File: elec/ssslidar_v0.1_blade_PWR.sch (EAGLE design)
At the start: 22 parts, among them P1 PIN_SMD_0.8X1_RECT, P10 PIN_SMD_0.8X1_RECT, P11 PIN_SMD_1X1_RECT, P12 PIN_SMD_0.8X1_RECT, P13 PIN_SMD_0.8X1_RECT, P16 PIN_SMD_0.8X1_RECT, P17 PIN_SMD_1X1_RECT, P18 PIN_SMD_0.8X1_RECT, P2 PIN_SMD_1X1_RECT, P3 PIN_SMD_0.8X1_RECT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

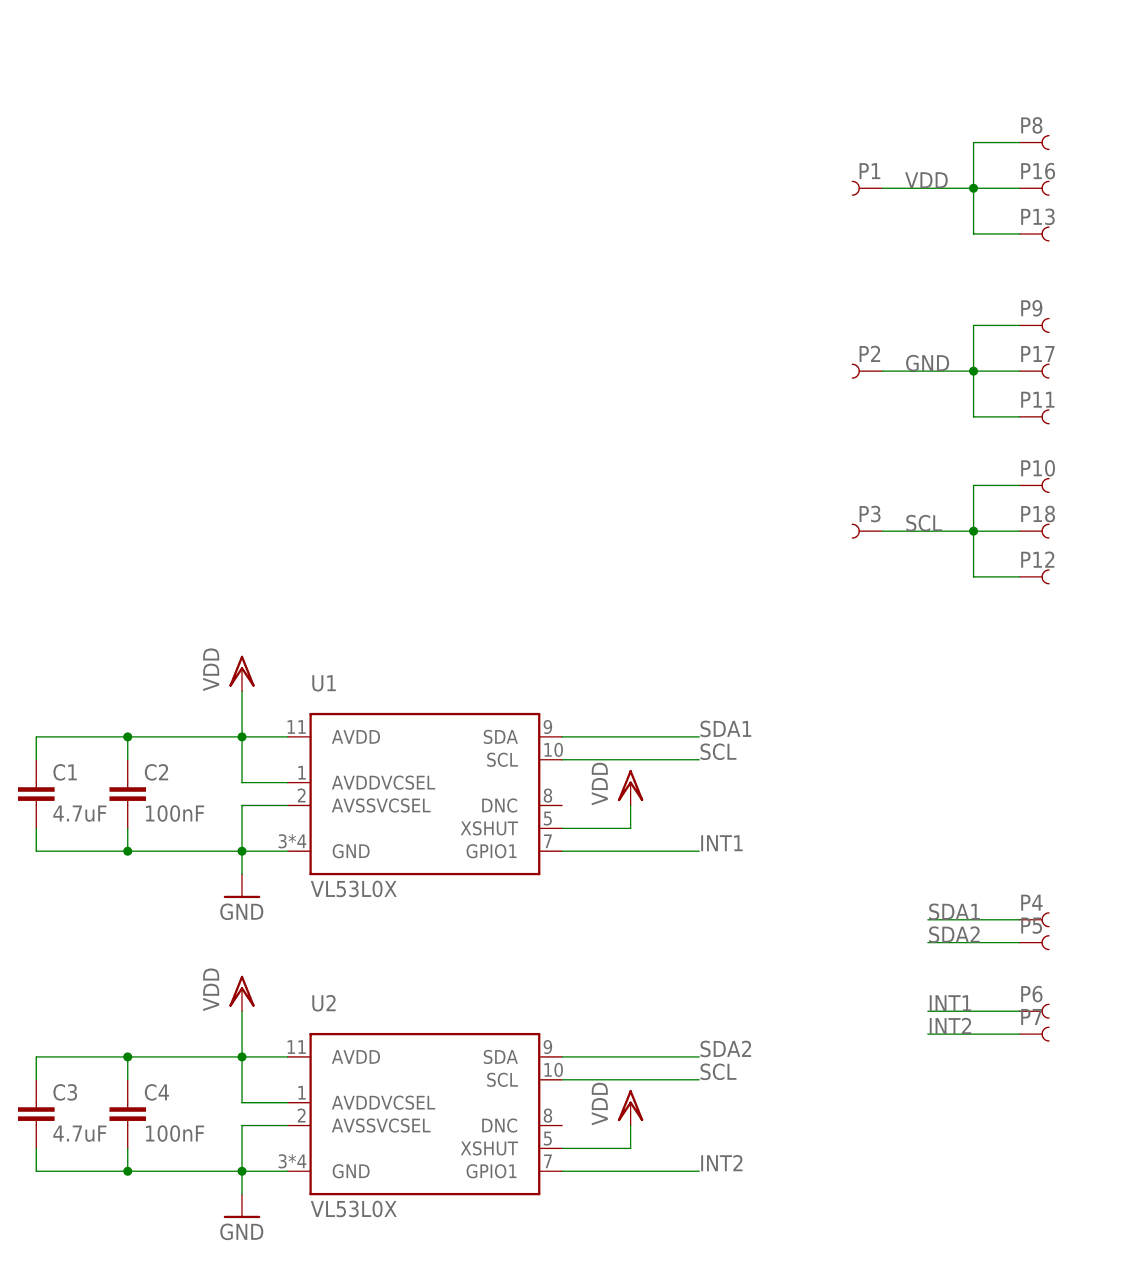
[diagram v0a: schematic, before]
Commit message: Working on main board Made blades longer to avoid too much occlusion from the main PCB (but we will still need to put the whole thing on a mast).
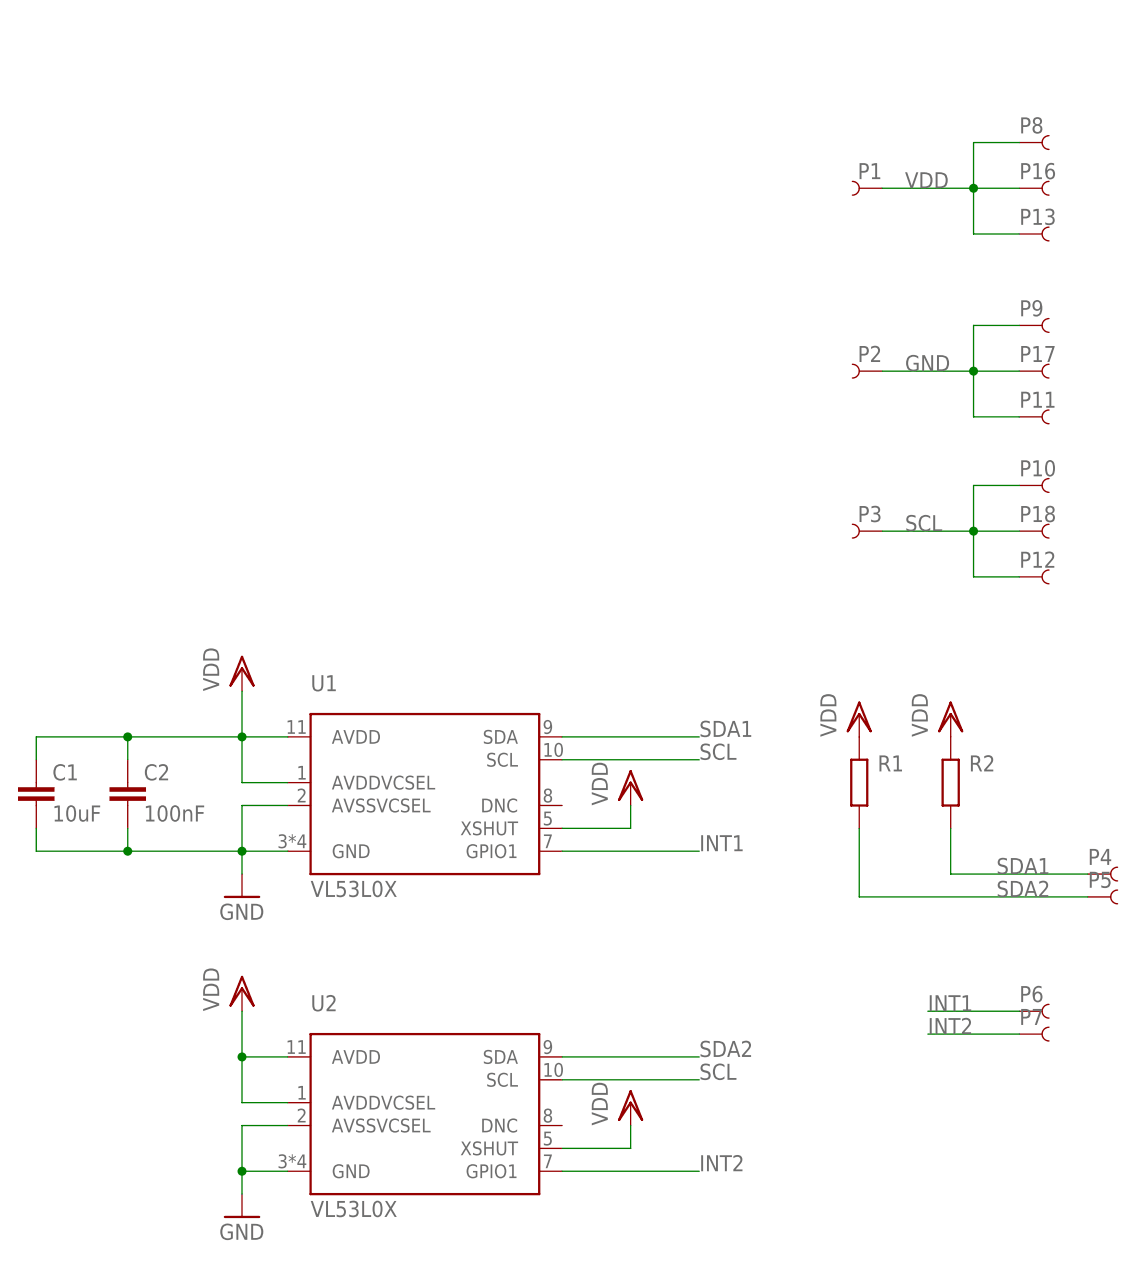
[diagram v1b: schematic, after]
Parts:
- removed C3: 4.7uF, Xevelabs:C0603
- removed C4: 100nF, Xevelabs:C0201
- added R1, R2: (no value), Xevelabs:R0402
- C1: value 4.7uF -> 10uF; device Xevelabs:C0603 -> Xevelabs:C0805
- C2: device Xevelabs:C0201 -> Xevelabs:C0402
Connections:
- net GND: no longer C3.2, C4.2
- net SDA1: now also R2.1
- net SDA2: now also R1.1
- net VDD: now also R1.2, R2.2; no longer C3.1, C4.1
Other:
- moved on the sheet: P4, P5
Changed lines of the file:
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@@
 <part name="GND1" library="supply1" deviceset="GND" device=""/>
 <part name="VDD1" library="supply1" deviceset="VDD" device=""/>
-<part name="C1" library="Xevelabs" deviceset="C" device="0603" value="4.7uF"/>
-<part name="C2" library="Xevelabs" deviceset="C" device="0201" value="100nF"/>
+<part name="C1" library="Xevelabs" deviceset="C" device="0805" value="10uF"/>
+<part name="C2" library="Xevelabs" deviceset="C" device="0402" value="100nF"/>
 <part name="VDD2" library="supply1" deviceset="VDD" device=""/>
 <part name="U2" library="VL53L0X" deviceset="VL53L0X" device=""/>
 <part name="GND2" library="supply1" deviceset="GND" device=""/>
 <part name="VDD3" library="supply1" deviceset="VDD" device=""/>
-<part name="C3" library="Xevelabs" deviceset="C" device="0603" value="4.7uF"/>
-<part name="C4" library="Xevelabs" deviceset="C" device="0201" value="100nF"/>
 <part name="VDD4" library="supply1" deviceset="VDD" device=""/>
 <part name="P1" library="Xevelabs" deviceset="PIN" device="_SMD_0.8X1_RECT" value="PIN_SMD_0.8X1_RECT"/>
@@
 <part name="P12" library="Xevelabs" deviceset="PIN" device="_SMD_0.8X1_RECT" value="PIN_SMD_0.8X1_RECT"/>
 <part name="P13" library="Xevelabs" deviceset="PIN" device="_SMD_0.8X1_RECT" value="PIN_SMD_0.8X1_RECT"/>
+<part name="R1" library="Xevelabs" deviceset="R" device="0402"/>
+<part name="R2" library="Xevelabs" deviceset="R" device="0402"/>
+<part name="VDD5" library="supply1" deviceset="VDD" device=""/>
+<part name="VDD6" library="supply1" deviceset="VDD" device=""/>
 </parts>
 <sheets>
@@
 <instance part="GND2" gate="1" x="27.94" y="5.08"/>
 <instance part="VDD3" gate="G$1" x="27.94" y="30.48"/>
-<instance part="C3" gate="G$1" x="5.08" y="15.24"/>
-<instance part="C4" gate="G$1" x="15.24" y="15.24"/>
 <instance part="VDD4" gate="G$1" x="71.12" y="17.78"/>
 <instance part="P1" gate="G$1" x="99.06" y="119.38" rot="MR0"/>
 <instance part="P2" gate="G$1" x="99.06" y="99.06" rot="MR0"/>
 <instance part="P3" gate="G$1" x="99.06" y="81.28" rot="MR0"/>
-<instance part="P4" gate="G$1" x="114.3" y="38.1"/>
-<instance part="P5" gate="G$1" x="114.3" y="35.56"/>
+<instance part="P4" gate="G$1" x="121.92" y="43.18"/>
+<instance part="P5" gate="G$1" x="121.92" y="40.64"/>
 <instance part="P6" gate="G$1" x="114.3" y="27.94"/>
 <instance part="P7" gate="G$1" x="114.3" y="25.4"/>
@@
 <instance part="P12" gate="G$1" x="114.3" y="76.2"/>
 <instance part="P13" gate="G$1" x="114.3" y="114.3"/>
+<instance part="R1" gate="G$1" x="96.52" y="53.34"/>
+<instance part="R2" gate="G$1" x="106.68" y="53.34"/>
+<instance part="VDD5" gate="G$1" x="96.52" y="60.96"/>
+<instance part="VDD6" gate="G$1" x="106.68" y="60.96"/>
 </instances>
 <busses>
@@
 <wire x1="27.94" y1="17.78" x2="27.94" y2="22.86" width="0.1524" layer="91"/>
 <junction x="27.94" y="22.86"/>
-<wire x1="27.94" y1="22.86" x2="15.24" y2="22.86" width="0.1524" layer="91"/>
-<pinref part="C4" gate="G$1" pin="1"/>
-<wire x1="15.24" y1="22.86" x2="15.24" y2="20.32" width="0.1524" layer="91"/>
-<pinref part="C3" gate="G$1" pin="1"/>
-<wire x1="15.24" y1="22.86" x2="5.08" y2="22.86" width="0.1524" layer="91"/>
-<wire x1="5.08" y1="22.86" x2="5.08" y2="20.32" width="0.1524" layer="91"/>
-<junction x="15.24" y="22.86"/>
 </segment>
 <segment>
@@
 <pinref part="P13" gate="G$1" pin="1"/>
 <wire x1="109.22" y1="114.3" x2="114.3" y2="114.3" width="0.1524" layer="91"/>
+</segment>
+<segment>
+<pinref part="R1" gate="G$1" pin="2"/>
+<pinref part="VDD5" gate="G$1" pin="VDD"/>
+</segment>
+<segment>
+<pinref part="R2" gate="G$1" pin="2"/>
+<pinref part="VDD6" gate="G$1" pin="VDD"/>
 </segment>
 </net>
@@
 <wire x1="27.94" y1="15.24" x2="27.94" y2="10.16" width="0.1524" layer="91"/>
 <junction x="27.94" y="10.16"/>
-<pinref part="C3" gate="G$1" pin="2"/>
-<wire x1="5.08" y1="12.7" x2="5.08" y2="10.16" width="0.1524" layer="91"/>
-<wire x1="5.08" y1="10.16" x2="15.24" y2="10.16" width="0.1524" layer="91"/>
-<pinref part="C4" gate="G$1" pin="2"/>
-<wire x1="15.24" y1="10.16" x2="27.94" y2="10.16" width="0.1524" layer="91"/>
-<wire x1="15.24" y1="12.7" x2="15.24" y2="10.16" width="0.1524" layer="91"/>
-<junction x="15.24" y="10.16"/>
 </segment>
 <segment>
@@
 <segment>
 <pinref part="P4" gate="G$1" pin="1"/>
-<wire x1="114.3" y1="38.1" x2="104.14" y2="38.1" width="0.1524" layer="91"/>
-<label x="104.14" y="38.1" size="1.778" layer="95"/>
+<wire x1="121.92" y1="43.18" x2="106.68" y2="43.18" width="0.1524" layer="91"/>
+<label x="111.76" y="43.18" size="1.778" layer="95"/>
+<pinref part="R2" gate="G$1" pin="1"/>
+<wire x1="106.68" y1="43.18" x2="106.68" y2="48.26" width="0.1524" layer="91"/>
 </segment>
 </net>
@@
 <segment>
 <pinref part="P5" gate="G$1" pin="1"/>
-<wire x1="114.3" y1="35.56" x2="104.14" y2="35.56" width="0.1524" layer="91"/>
-<label x="104.14" y="35.56" size="1.778" layer="95"/>
-</segment>
-</net>
+<label x="111.76" y="40.64" size="1.778" layer="95"/>
+<pinref part="R1" gate="G$1" pin="1"/>
+<wire x1="121.92" y1="40.64" x2="96.52" y2="40.64" width="0.1524" layer="91"/>
+<wire x1="96.52" y1="40.64" x2="96.52" y2="48.26" width="0.1524" layer="91"/>
+</segment>
+</net>
